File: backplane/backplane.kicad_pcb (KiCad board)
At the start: 2 copper layers, 142.8 x 197.5 mm, 20 parts, among them J1 Conn_01x10, J10 Conn_01x10, J11 Conn_01x10, J2 Conn_01x10, J3 48V in, J4 48V in, J5 Conn_01x10, J6 Conn_01x10, J7 Conn_01x10, J8 Conn_01x10, J9 Conn_01x10

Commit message: ground plane
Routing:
- added copper zone on B.Cu, net /12v_1
- added copper zone on B.Cu, net /12v_2
- added copper zone on B.Cu, net /12v_3
- added copper zone on B.Cu, net /24v
- added copper zone on B.Cu, net /48v
- added copper zone on B.Cu, net /5v
- added copper zone on B.Cu, net GND1
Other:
- board text added: "2024-backplane"
- board text added: "AUX"
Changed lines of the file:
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@@
   (gr_line (start 115 146) (end 115 109)
     (stroke (width 0.15) (type default)) (layer "F.SilkS"))
+  (gr_line (start 115 160.25) (end 115 152.75)
+    (stroke (width 0.15) (type default)) (layer "F.SilkS"))
   (gr_line (start 115 105.5) (end 115 68.5)
     (stroke (width 0.15) (type default)) (layer "F.SilkS"))
-  (gr_line (start 241 159.76) (end 241 226.68)
-    (stroke (width 0.15) (type default)) (layer "F.SilkS"))
-  (gr_line (start 115 160.84) (end 115 148.76)
-    (stroke (width 0.15) (type default)) (layer "F.SilkS"))
-  (gr_line (start 241 159.76) (end 241 144.76)
-    (stroke (width 0.15) (type default)) (layer "F.SilkS"))
-  (gr_line (start 115 227.76) (end 115 233.76)
-    (stroke (width 0.15) (type default)) (layer "F.SilkS"))
-  (gr_line (start 115 227.76) (end 115 160.84)
+  (gr_line (start 241 147.25) (end 241 154.5)
+    (stroke (width 0.15) (type default)) (layer "F.SilkS"))
+  (gr_line (start 241 162.25) (end 241 221)
+    (stroke (width 0.15) (type default)) (layer "F.SilkS"))
+  (gr_line (start 115 225.5) (end 115 165.25)
     (stroke (width 0.15) (type default)) (layer "F.SilkS"))
   (gr_line (start 240.75 142.25) (end 240.75 104.25)
@@
     (effects (font (size 4 4) (thickness 0.3) bold) (justify left bottom))
   )
+  (gr_text "AUX" (at 113.25 162 90) (layer "F.SilkS")
+    (effects (font (size 4 4) (thickness 0.3) bold) (justify left bottom))
+  )
   (gr_text "ESC" (at 247.25 131.75 90) (layer "F.SilkS")
     (effects (font (size 4 4) (thickness 0.3) bold) (justify left bottom))
   )
-  (gr_text "POWER" (at 247.25 191.75 90) (layer "F.SilkS")
-    (effects (font (size 4 4) (thickness 0.3) bold) (justify left bottom))
-  )
-  (gr_text "48V IN" (at 197.25 245 180) (layer "F.SilkS")
+  (gr_text "POWER" (at 247.25 200.75 90) (layer "F.SilkS")
+    (effects (font (size 4 4) (thickness 0.3) bold) (justify left bottom))
+  )
+  (gr_text "48V IN" (at 156.75 247) (layer "F.SilkS")
     (effects (font (size 2 2) (thickness 0.15)) (justify left bottom))
   )
-  (gr_text "POWER" (at 113.25 191.75 90) (layer "F.SilkS")
-    (effects (font (size 4 4) (thickness 0.3) bold) (justify left bottom))
-  )
-  (gr_text "48V IN" (at 167 245 180) (layer "F.SilkS")
+  (gr_text "POWER" (at 113.25 200.75 90) (layer "F.SilkS")
+    (effects (font (size 4 4) (thickness 0.3) bold) (justify left bottom))
+  )
+  (gr_text "48V IN" (at 187 247) (layer "F.SilkS")
     (effects (font (size 2 2) (thickness 0.15)) (justify left bottom))
+  )
+  (gr_text "2024-backplane" (at 206.5 231.25) (layer "F.SilkS")
+    (effects (font (size 3 3) (thickness 0.15)) (justify left bottom))
+  )
+  (gr_text "AUX" (at 247.25 156.25 90) (layer "F.SilkS")
+    (effects (font (size 4 4) (thickness 0.3) bold) (justify left bottom))
   )
   (gr_text "MAIN" (at 113.25 91.25 90) (layer "F.SilkS")
@@
   (segment (start 226.125 200.73) (end 226.125 198) (width 0.25) (layer "F.Cu") (net 10))
   (segment (start 226.115 107.17) (end 226.115 64.73) (width 0.25) (layer "F.Cu") (net 10))
-  (zone (net 11) (net_name "/48v") (layer "F.Cu") (hatch edge 0.5)
+  (zone (net 11) (net_name "/48v") (layers "F&B.Cu") (hatch edge 0.5)
     (priority 5)
-    (connect_pads (clearance 0.5))
+    (connect_pads yes (clearance 0.5))
     (min_thickness 0.25) (filled_areas_thickness no)
     (fill yes (thermal_gap 0.5) (thermal_bridge_width 0.5))
@@
     )
   )
-  (zone (net 12) (net_name "GND1") (layer "F.Cu") (hatch edge 0.5)
-    (priority 6)
-    (connect_pads yes (clearance 0.5))
-    (min_thickness 0.25) (filled_areas_thickness no)
-    (fill yes (thermal_gap 0.5) (thermal_bridge_width 0.5))
-    (polygon
-      (pts
-        (xy 163 232.25)
-        (xy 163.25 243.75)
-        (xy 181.5 243.421595)
-        (xy 181.545619 231.75)
-        (xy 193.5 231.75)
-        (xy 193.5 243)
-        (xy 202.75 243)
-        (xy 202.75 234)
-        (xy 192.25 223.5)
-        (xy 181 223.5)
-        (xy 180.25 222.75)
-        (xy 180.25 65.5)
-        (xy 175.5 65.5)
-        (xy 175.5 223.5)
-        (xy 175.25 223.75)
-        (xy 136 223.75)
-        (xy 136 65.25)
-        (xy 125.75 65.25)
-        (xy 125.5 65.5)
-        (xy 126 223)
-        (xy 135 231.603918)
-      )
-    )
-  )
-  (zone (net 13) (net_name "/12v_1") (layer "F.Cu") (hatch edge 0.5)
+  (zone (net 12) (net_name "GND1") (layers "F&B.Cu") (hatch edge 0.5)
+    (connect_pads yes (clearance 0.5))
+    (min_thickness 0.25) (filled_areas_thickness no)
+    (fill yes (thermal_gap 0.5) (thermal_bridge_width 0.5))
+    (polygon
+      (pts
+        (xy 248 252)
+        (xy 106 252)
+        (xy 106 56.25)
+        (xy 107.25 55)
+        (xy 248.25 55)
+        (xy 248.75 55.5)
+        (xy 248.75 251.25)
+      )
+    )
+  )
+  (zone (net 13) (net_name "/12v_1") (layers "F&B.Cu") (hatch edge 0.5)
+    (priority 1)
     (connect_pads yes (clearance 0.5))
     (min_thickness 0.25) (filled_areas_thickness no)
@@
     )
   )
-  (zone (net 15) (net_name "/12v_3") (layer "F.Cu") (hatch edge 0.5)
+  (zone (net 15) (net_name "/12v_3") (layers "F&B.Cu") (hatch edge 0.5)
     (priority 2)
     (connect_pads yes (clearance 0.5))
@@
     )
   )
-  (zone (net 16) (net_name "/24v") (layer "F.Cu") (hatch edge 0.5)
+  (zone (net 16) (net_name "/24v") (layers "F&B.Cu") (hatch edge 0.5)
     (priority 4)
     (connect_pads yes (clearance 0.5))
@@
         (xy 169.75 222.5)
         (xy 169.75 65.25)
-        (xy 175 70.5)
+        (xy 175 65.25)
         (xy 175 222.75)
         (xy 170 222.75)
@@
     )
   )
-  (zone (net 17) (net_name "/5v") (layer "F.Cu") (hatch edge 0.5)
+  (zone (net 17) (net_name "/5v") (layers "F&B.Cu") (hatch edge 0.5)
     (priority 3)
     (connect_pads yes (clearance 0.5))
@@
     )
   )
-  (zone (net 14) (net_name "/12v_2") (layer "F.Cu") (hatch edge 0.5)
+  (zone (net 14) (net_name "/12v_2") (layers "F&B.Cu") (hatch edge 0.5)
     (priority 1)
     (connect_pads yes (clearance 0.5))

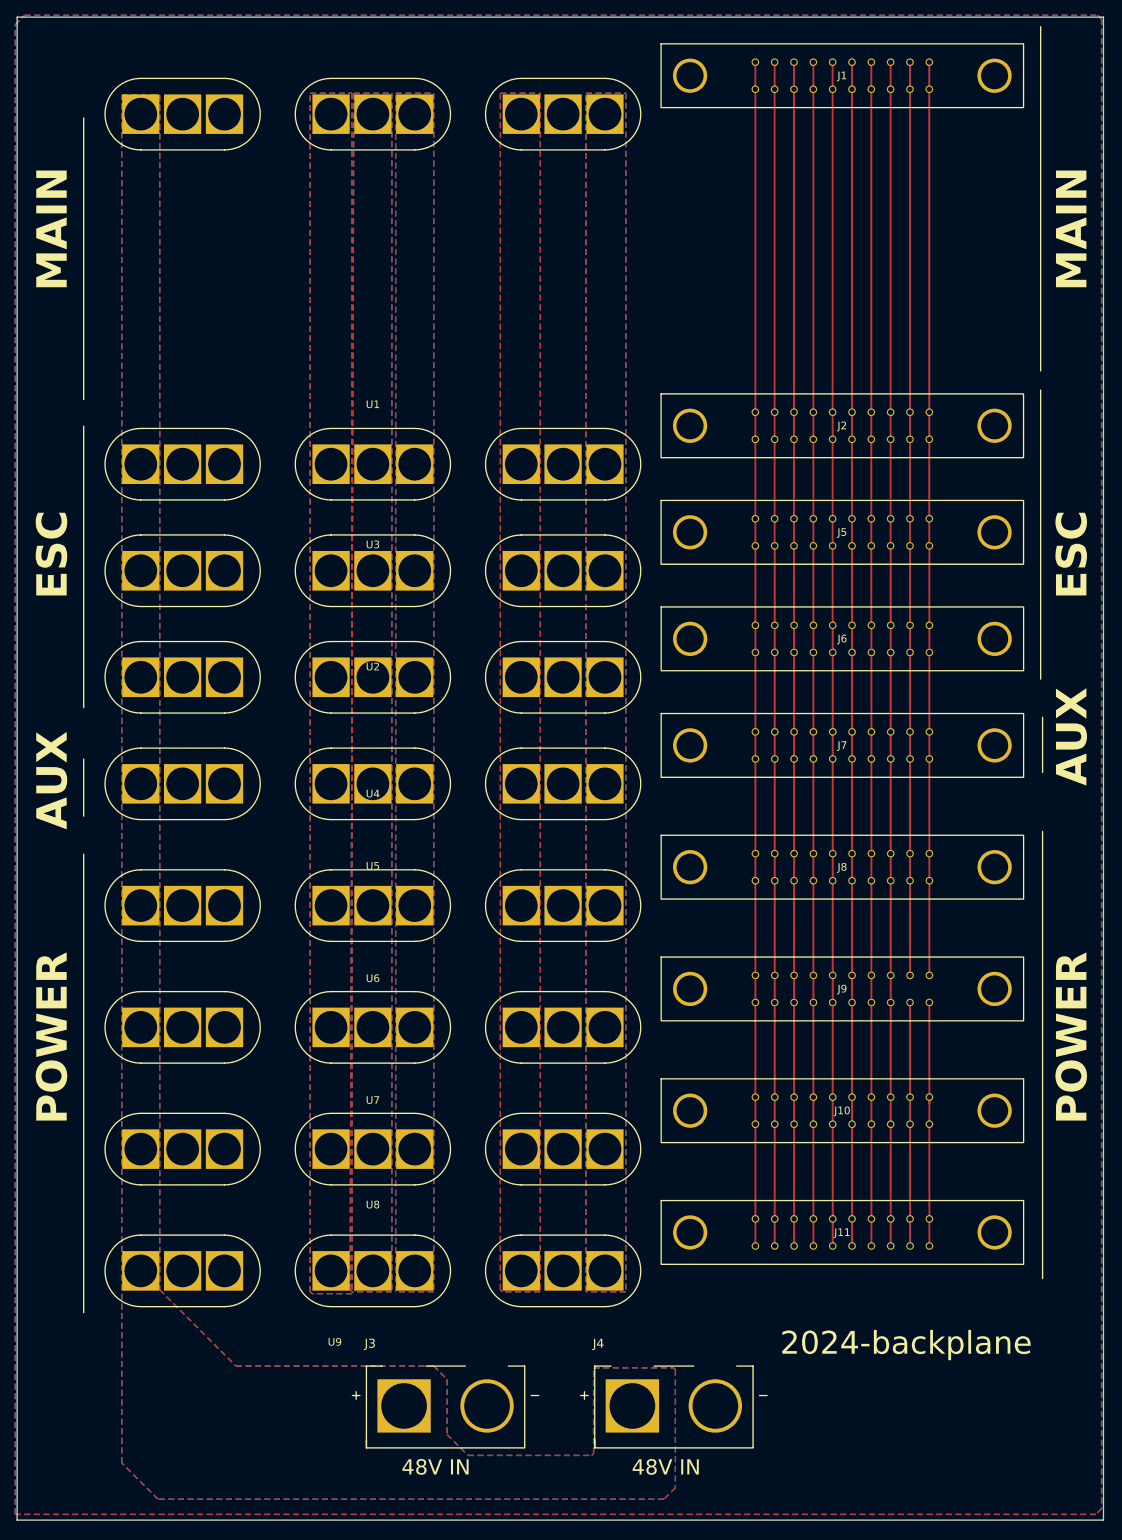
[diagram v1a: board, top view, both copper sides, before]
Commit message: added 3d models, cleaned up silk screen and added some voltage indicators
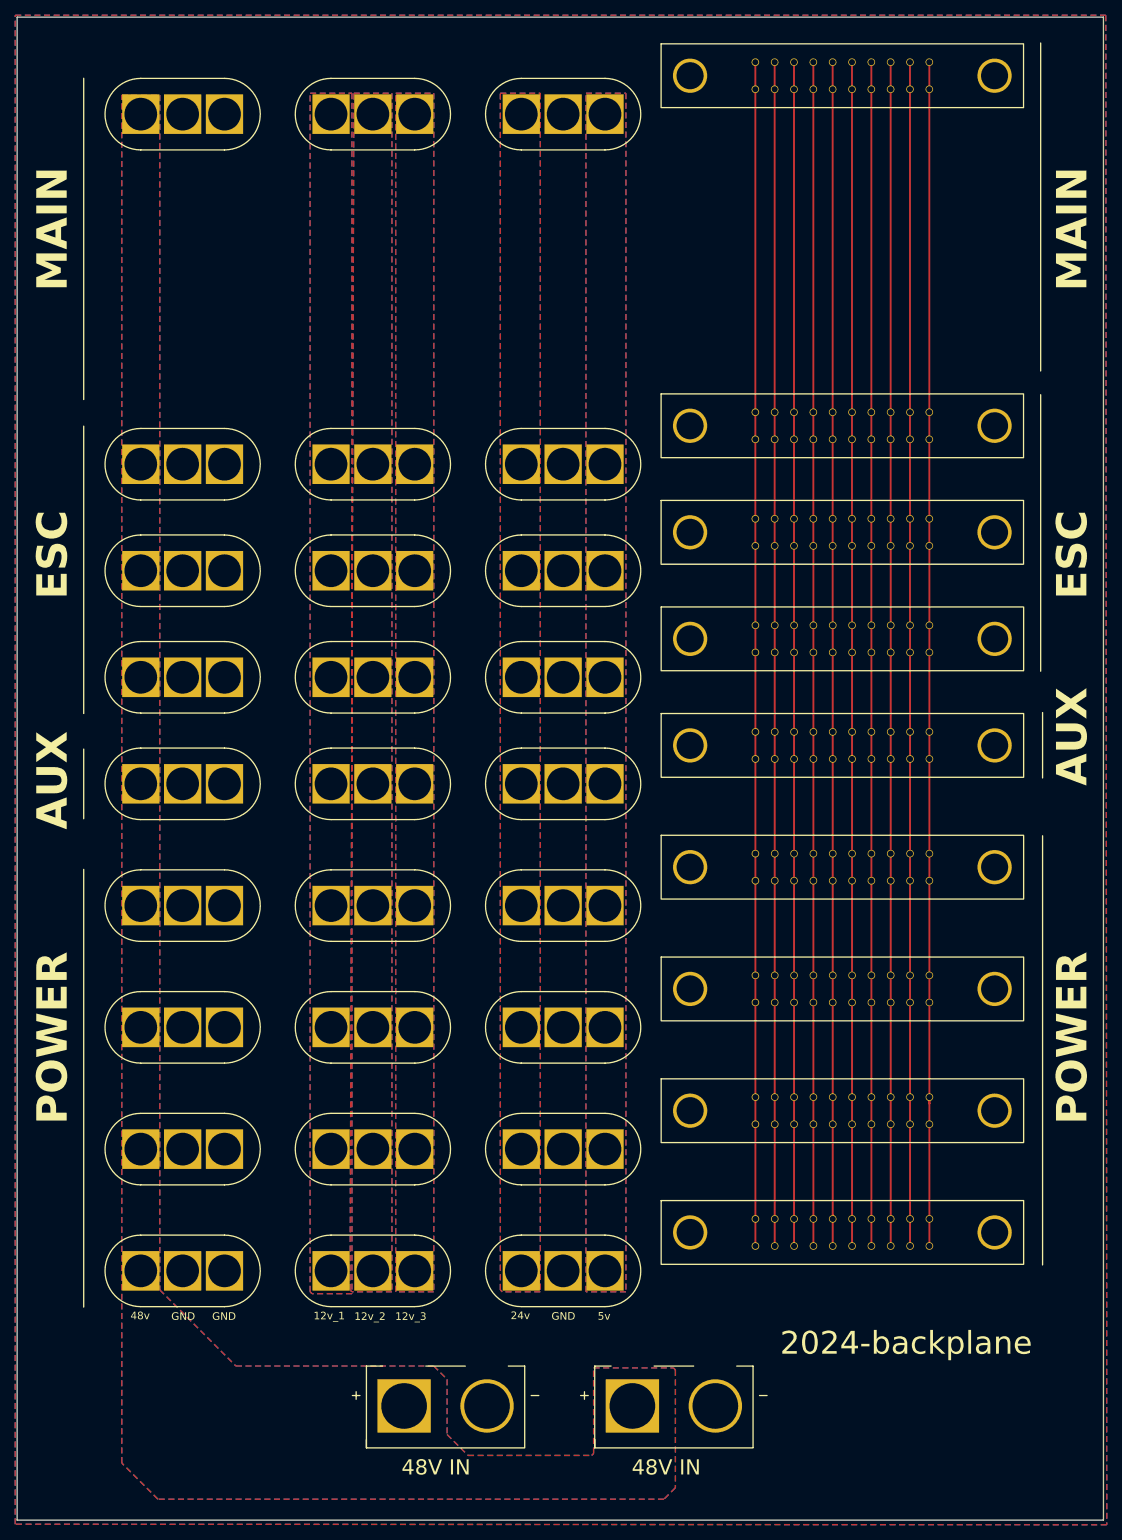
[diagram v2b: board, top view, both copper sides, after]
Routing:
- net /j: track 152.8 -> 156.4 mm
- net /i: track 152.0 -> 155.6 mm
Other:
- board text added: "12v_1"
- board text added: "12v_2"
- board text added: "12v_3"
- board text added: "24v"
- board text added: "48v"
- board text added: "5v"
- board text added: "GND"

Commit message: little tweaks
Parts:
- renumbered J3 to J
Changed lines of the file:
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@@
     (property "ki_description" "Generic connector, single row, 01x02, script generated (kicad-library-utils/schlib/autogen/connector/)")
     (property "ki_keywords" "connector")
-    (fp_text reference "J3" (at -10.9 -7.645) (layer "F.SilkS") hide
+    (attr through_hole)
+    (fp_text reference "J" (at -10.9 -7.645) (layer "F.SilkS") hide
         (effects (font (size 1.1684 1.1684) (thickness 0.1016)) (justify left bottom))
     )
